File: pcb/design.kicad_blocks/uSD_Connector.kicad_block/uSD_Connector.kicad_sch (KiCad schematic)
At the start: 4 parts, among them J3 0472192001

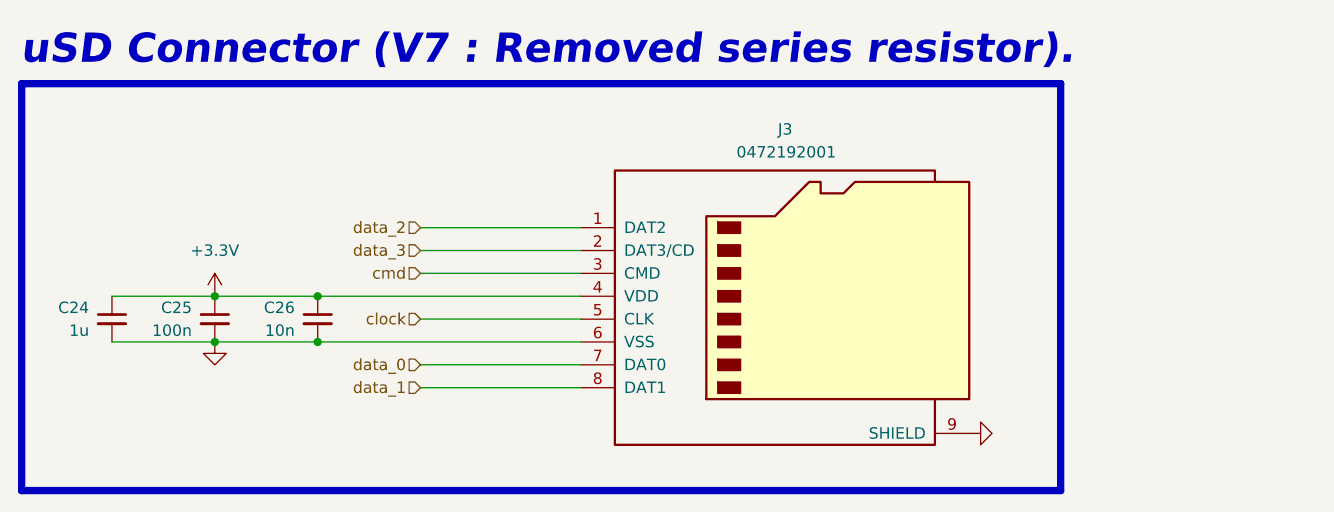
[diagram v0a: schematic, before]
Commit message: Fixing errata of missing pull-up resistors on `CMD` and `DAT0` lines of uSD connector.
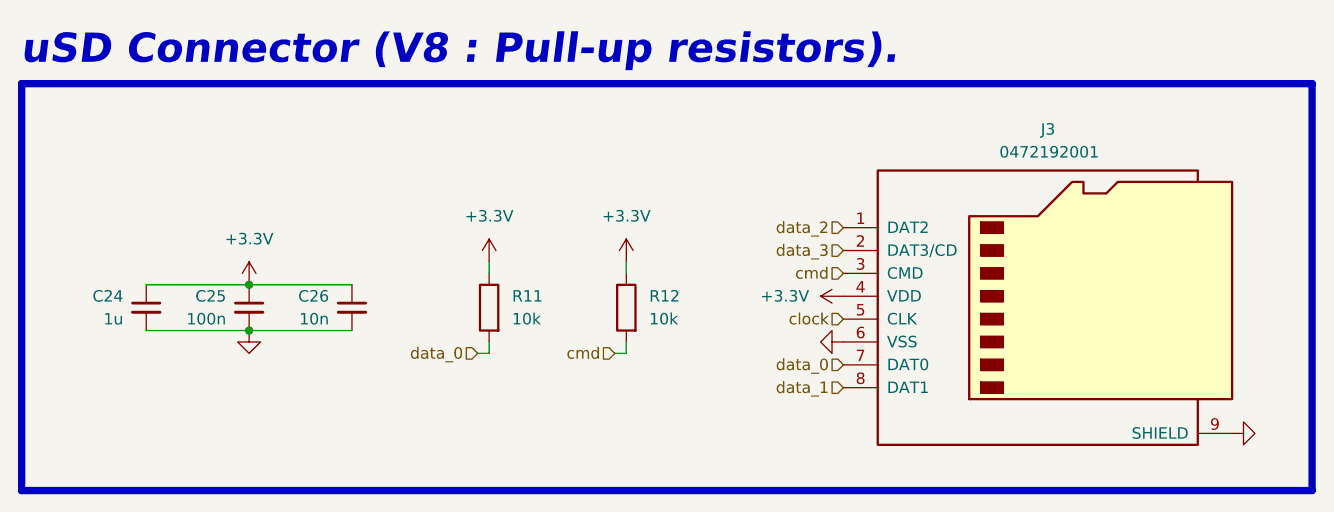
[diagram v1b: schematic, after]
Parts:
- added R11, R12: 10k, Resistor_SMD:R_1206_3216Metric_Pad1.30x1.75mm_HandSolder, symbol Device:R
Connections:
- net +3.3V: now also R11.1, R12.1
- net cmd: now also R12.2
- net data_0: now also R11.2
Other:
- note added: "uSD Connector (V8 : Pull-up resistors)."
- note removed: "uSD Connector (V7 : Removed series resistor)."
- moved on the sheet: C24, C25, C26, J3
